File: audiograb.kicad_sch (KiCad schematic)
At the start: 6 parts, among them J1 USB_C_Receptacle_USB2.0_16P, U12 IP4220CZ6F

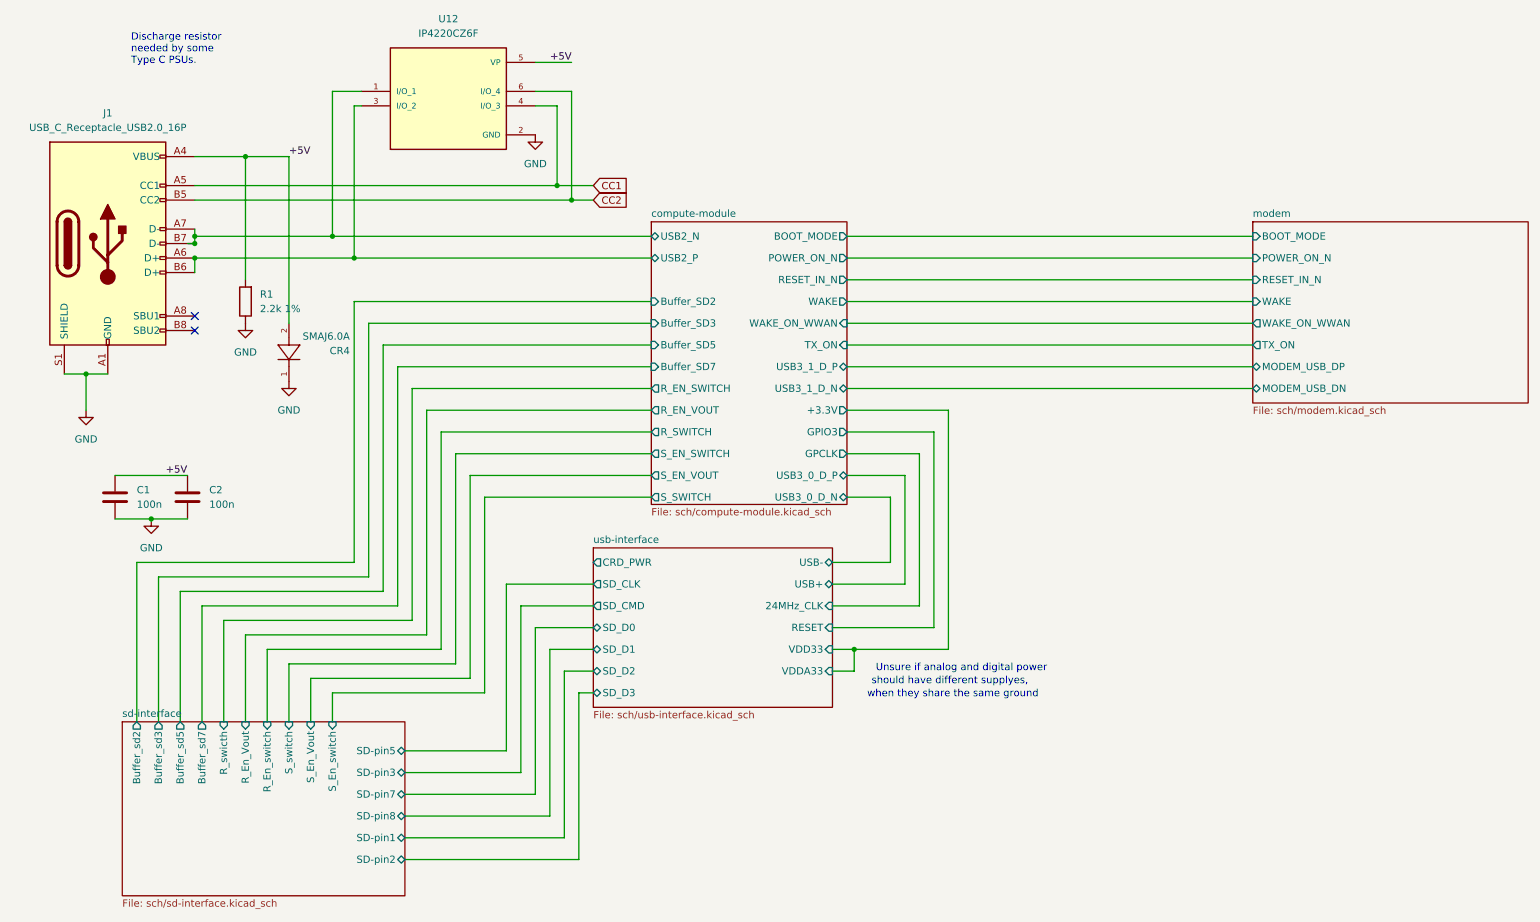
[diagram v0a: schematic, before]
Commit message: added ports to powersupply
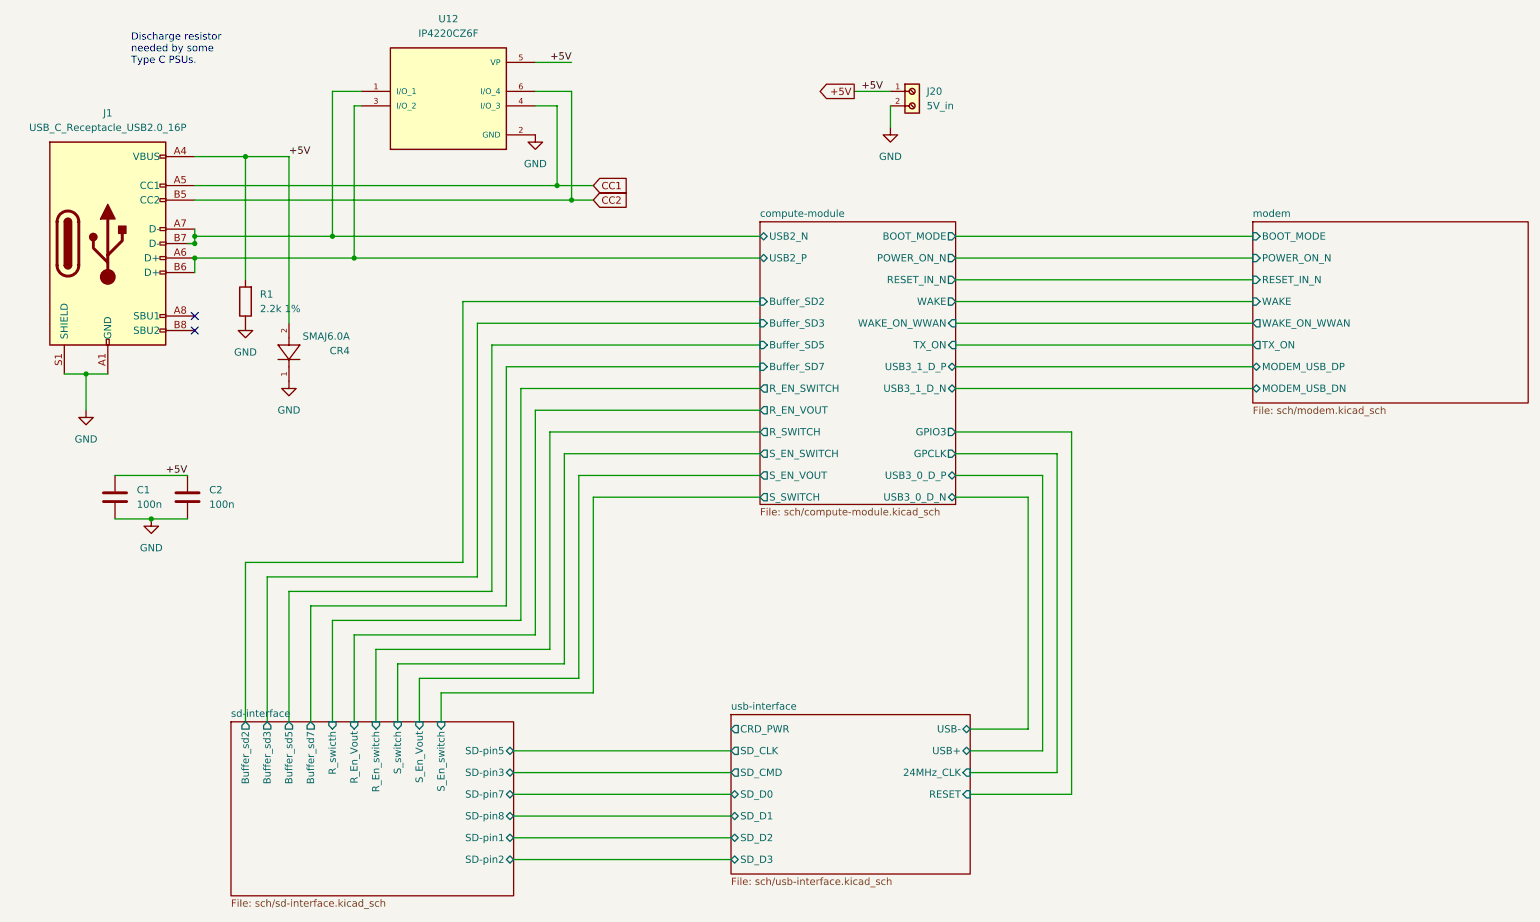
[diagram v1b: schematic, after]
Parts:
- added J20: 5V_in, 691137710002:691137710002, symbol 691137710002:691137710002
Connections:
- net +5V: now also J20.1
- net GND: now also J20.2
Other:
- sheet compute-module ports: added none; removed +3.3V
- sheet usb-interface ports: added none; removed VDD33, VDDA33
- note removed: "Unsure if analog and digital power"
- note removed: "should have different supplyes,"
- note removed: "when they share the same ground"

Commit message: fix annotation and clean up schematics
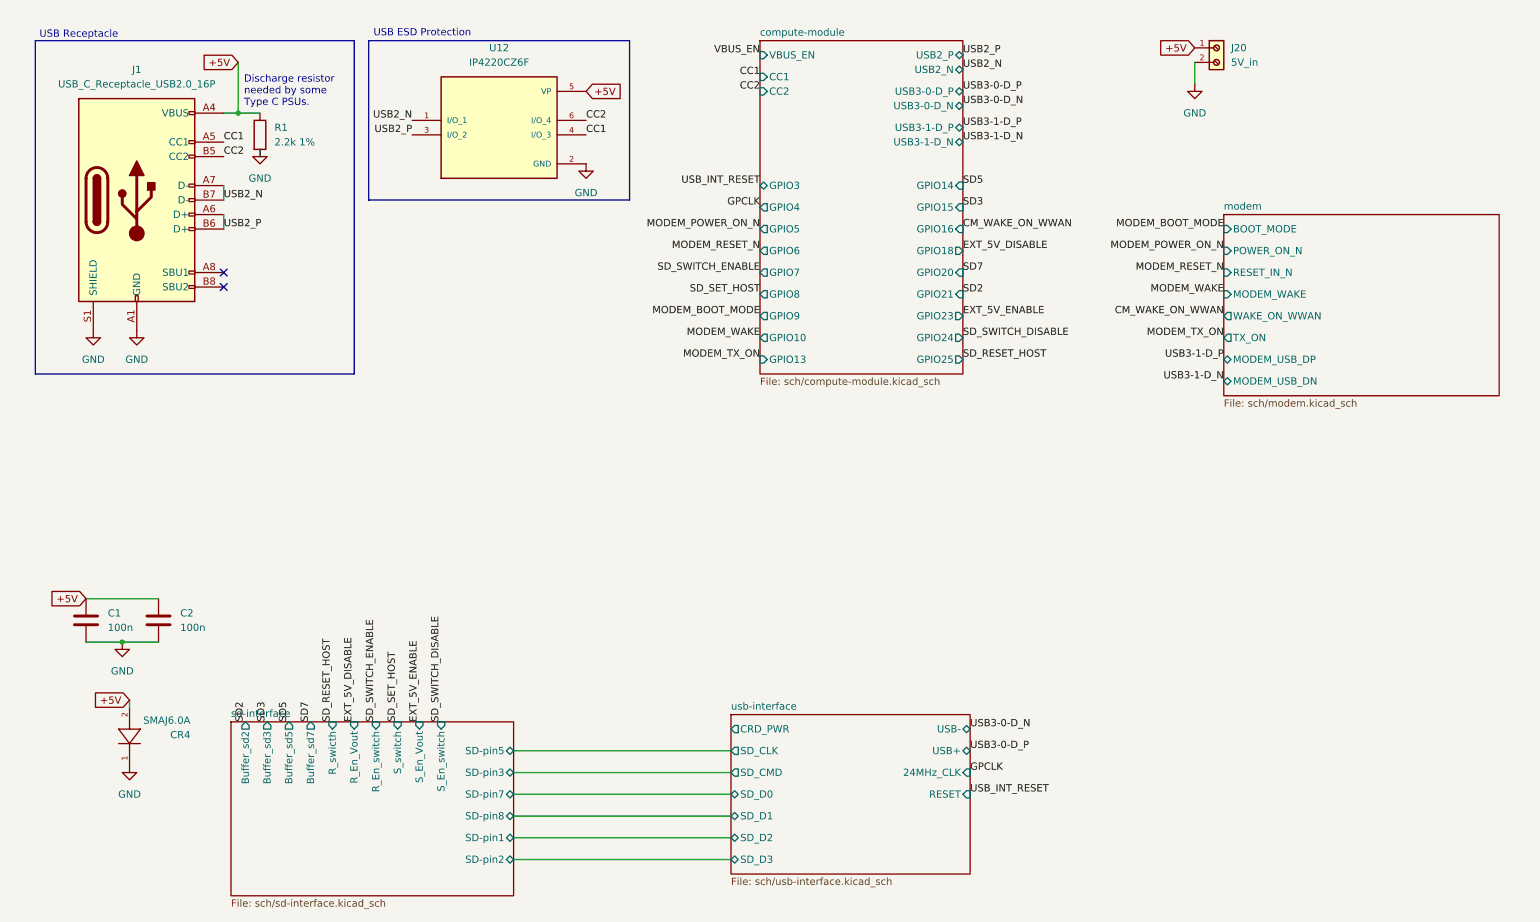
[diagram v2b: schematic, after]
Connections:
- net +5V: now also R1.1; no longer R1.2
- net GND: now also R1.2; no longer R1.1
- net compute-module/USB2_N renamed USB2_N
- net compute-module/USB2_P renamed USB2_P
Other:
- sheet compute-module ports: added CC1, CC2, GPIO10, GPIO13, GPIO14, GPIO15, GPIO16, GPIO18, GPIO20, GPIO21, GPIO23, GPIO24, GPIO25, GPIO4, GPIO5, GPIO6, GPIO7, GPIO8, GPIO9, USB3-0-D_N, USB3-0-D_P, USB3-1-D_N, USB3-1-D_P, VBUS_EN; removed BOOT_MODE, Buffer_SD2, Buffer_SD3, Buffer_SD5, Buffer_SD7, GPCLK, POWER_ON_N, RESET_IN_N, R_EN_SWITCH, R_EN_VOUT, R_SWITCH, S_EN_SWITCH, S_EN_VOUT, S_SWITCH, TX_ON, USB3_0_D_N, USB3_0_D_P, USB3_1_D_N, USB3_1_D_P, WAKE, WAKE_ON_WWAN
- sheet modem ports: added MODEM_WAKE; removed WAKE
- note added: "USB ESD Protection"
- note added: "USB Receptacle"
- moved on the sheet: C1, C2, CR4, J1, J20, R1, U12

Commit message: started pcb design
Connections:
- net CC2: now also U12.3 (I/O_2); no longer U12.6 (I/O_4)
- net USB2_N: now also U12.6 (I/O_4); no longer U12.1 (I/O_1)
- net USB2_P: now also U12.1 (I/O_1); no longer U12.3 (I/O_2)
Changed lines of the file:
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@@
 	)
 	(label "USB2_P"
-		(at 81.28 34.29 180)
+		(at 81.28 31.75 180)
 		(effects
 			(font
@@
 	)
 	(label "CC2"
-		(at 111.76 31.75 0)
-		(effects
-			(font
-				(size 1.27 1.27)
-			)
-			(justify left bottom)
+		(at 81.28 34.29 180)
+		(effects
+			(font
+				(size 1.27 1.27)
+			)
+			(justify right bottom)
 		)
 	)
@@
 	)
 	(label "USB2_N"
-		(at 81.28 31.75 180)
-		(effects
-			(font
-				(size 1.27 1.27)
-			)
-			(justify right bottom)
-		)
-	)
+		(at 111.76 31.75 0)
+		(effects
+			(font
+				(size 1.27 1.27)
+			)
+			(justify left bottom)
+		)
+	)

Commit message: work pcb about 70 percent
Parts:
- removed J20: 5V_in, 691137710002:691137710002, symbol 691137710002:691137710002
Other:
- sheet modem ports: added WAKE_ON_WWAN_port; removed WAKE_ON_WWAN
- note added: "bytta navn for å unngaa label konflikt"

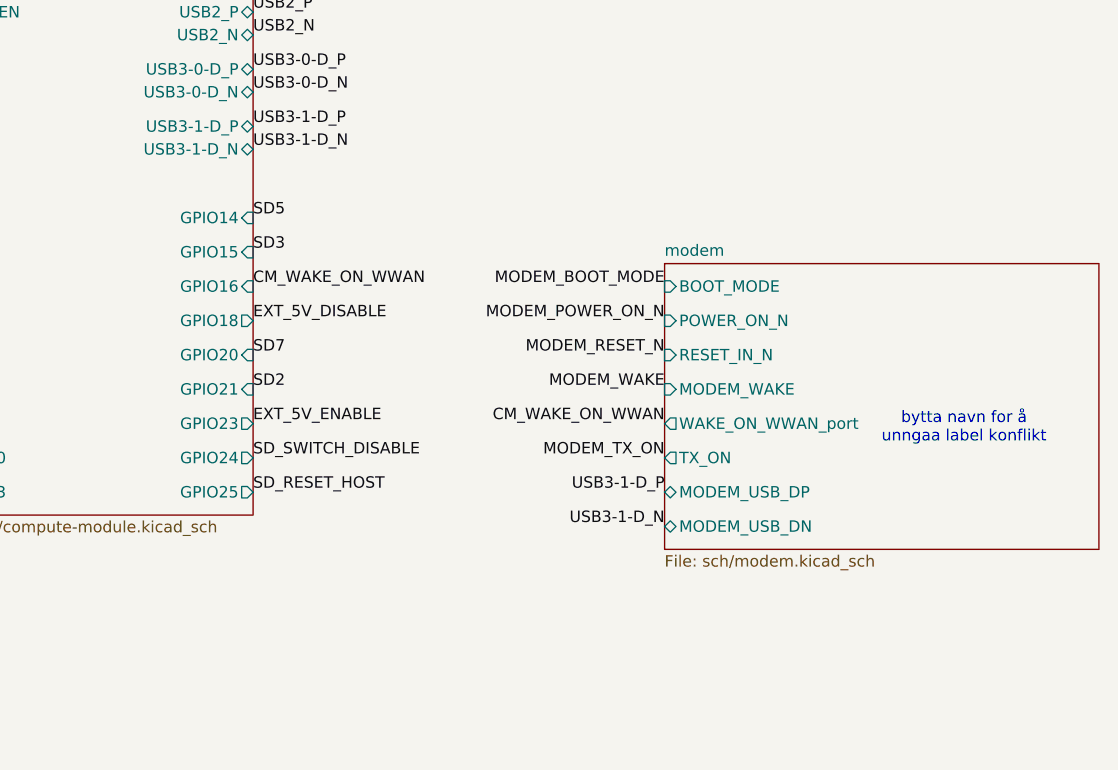
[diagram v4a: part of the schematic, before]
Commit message: partially route the powerlines
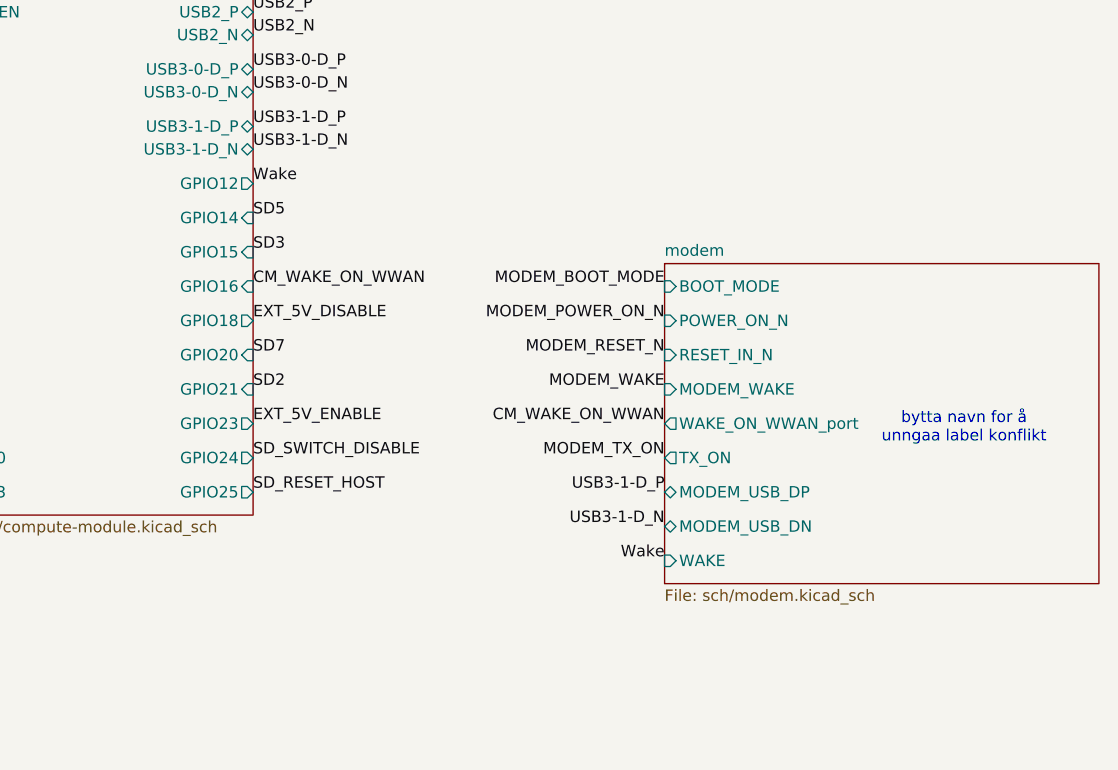
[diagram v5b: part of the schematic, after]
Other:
- sheet compute-module ports: added GPIO12; removed none
- sheet modem ports: added WAKE; removed none
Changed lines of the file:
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@@
+		)
+	)
+	(label "Wake"
+		(at 223.52 81.28 180)
+		(effects
+			(font
+				(size 1.27 1.27)
+			)
+			(justify right bottom)
 		)
 	)
 	(label "SD_RESET_HOST"
 		(at 67.31 137.16 90)
+		(effects
+			(font
+				(size 1.27 1.27)
+			)
+			(justify left bottom)
+		)
+	)
+	(label "Wake"
+		(at 177.8 39.37 0)
 		(effects
 			(font
@@
 	(sheet
 		(at 223.52 48.26)
-		(size 48.26 31.75)
+		(size 48.26 35.56)
 		(exclude_from_sim no)
 		(in_bom yes)
@@
 		)
 		(property "Sheetfile" "sch/modem.kicad_sch"
-			(at 223.52 80.5946 0)
+			(at 223.52 84.4046 0)
 			(effects
 				(font
@@
 		(pin "WAKE_ON_WWAN_port" output
 			(at 223.52 66.04 180)
+			(effects
+				(font
+					(size 1.27 1.27)
+				)
+				(justify left)
+			)
+		)
+		(pin "WAKE" input
+			(at 223.52 81.28 180)
 			(effects
 				(font
@@
 			)
 		)
+		(pin "GPIO12" output
+			(at 177.8 39.37 0)
+			(effects
+				(font
+					(size 1.27 1.27)
+				)
+				(justify right)
+			)
+		)

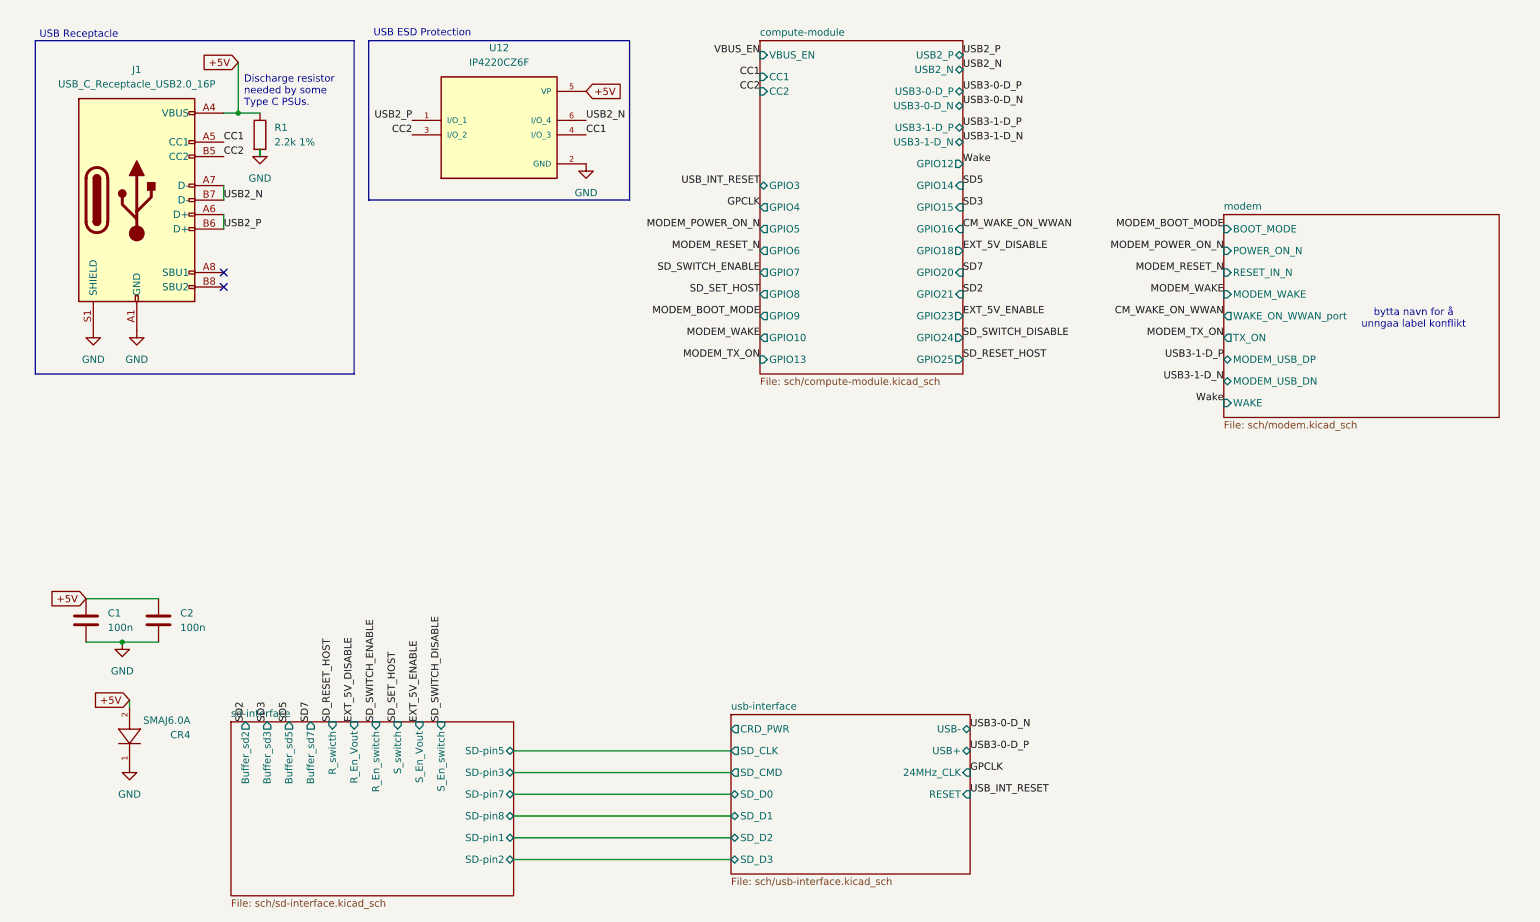
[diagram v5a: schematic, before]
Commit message: powergrid complete, still missing antennas
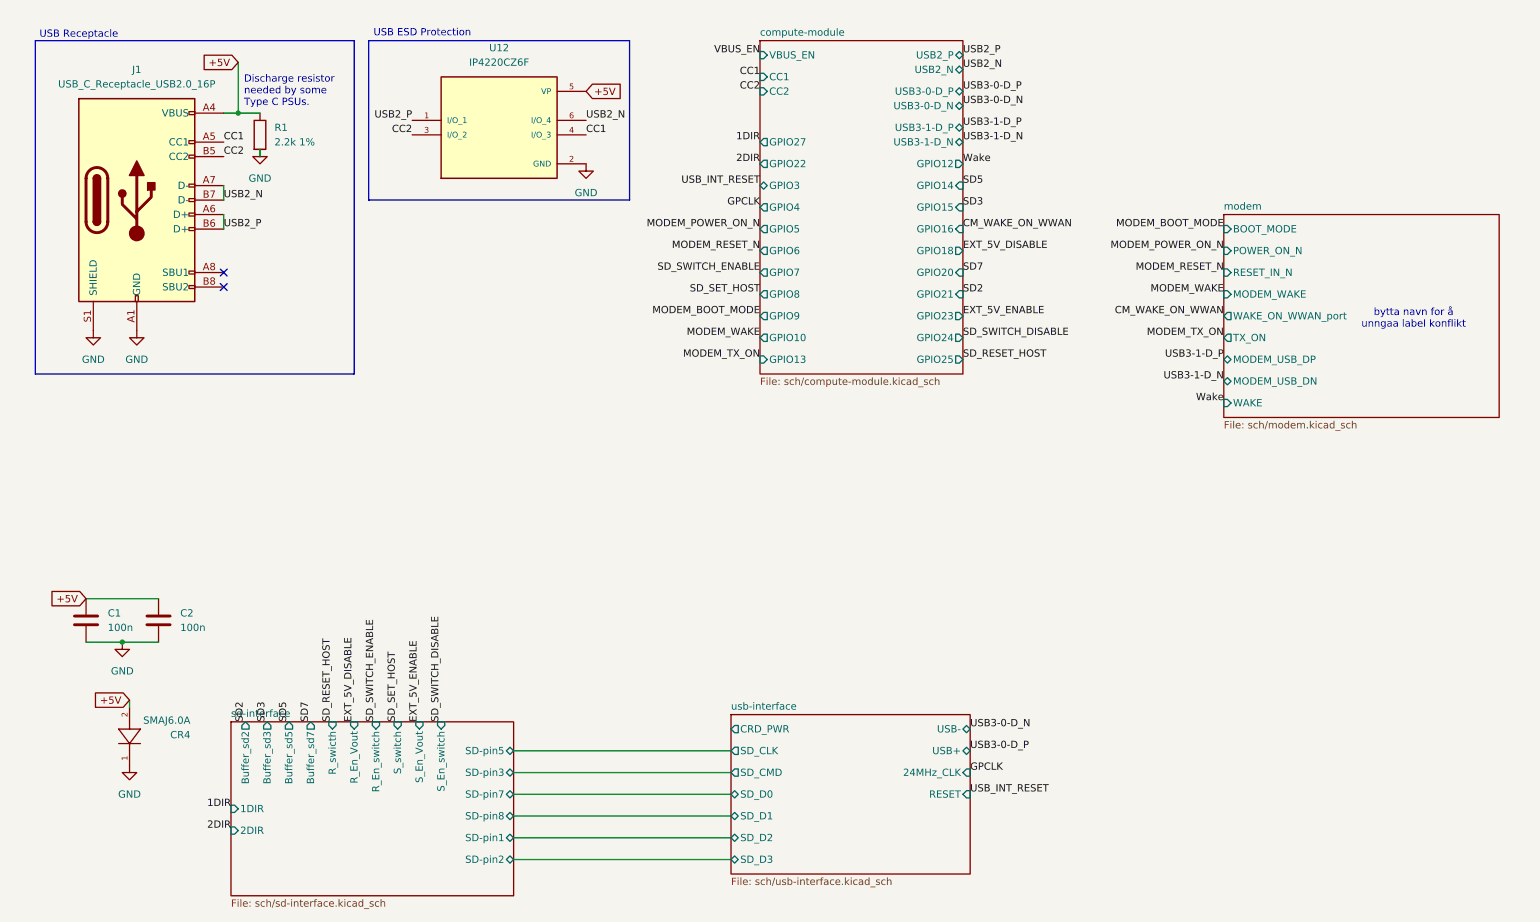
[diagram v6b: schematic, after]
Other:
- sheet compute-module ports: added GPIO22, GPIO27; removed none
- sheet sd-interface ports: added 1DIR, 2DIR; removed none
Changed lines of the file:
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@@
+		)
+	)
+	(label "2DIR"
+		(at 142.24 39.37 180)
+		(effects
+			(font
+				(size 1.27 1.27)
+			)
+			(justify right bottom)
 		)
 	)
@@
 		)
 	)
+	(label "1DIR"
+		(at 142.24 35.56 180)
+		(effects
+			(font
+				(size 1.27 1.27)
+			)
+			(justify right bottom)
+		)
+	)
 	(label "SD_RESET_HOST"
 		(at 177.8 73.66 0)
@@
 		)
 	)
+	(label "2DIR"
+		(at 49.53 156.21 180)
+		(effects
+			(font
+				(size 1.27 1.27)
+			)
+			(justify right bottom)
+		)
+	)
 	(label "MODEM_WAKE"
 		(at 142.24 69.85 180)
@@
 	(label "MODEM_RESET_N"
 		(at 223.52 58.42 180)
+		(effects
+			(font
+				(size 1.27 1.27)
+			)
+			(justify right bottom)
+		)
+	)
+	(label "1DIR"
+		(at 49.53 152.4 180)
 		(effects
 			(font
@@
 			)
 		)
+		(pin "1DIR" input
+			(at 49.53 152.4 180)
+			(effects
+				(font
+					(size 1.27 1.27)
+				)
+				(justify left)
+			)
+		)
+		(pin "2DIR" input
+			(at 49.53 156.21 180)
+			(effects
+				(font
+					(size 1.27 1.27)
+				)
+				(justify left)
+			)
+		)
 		(instances
 			(project "audiograb"
@@
 			)
 		)
+		(pin "GPIO22" output
+			(at 142.24 39.37 180)
+			(effects
+				(font
+					(size 1.27 1.27)
+				)
+				(justify left)
+			)
+		)
+		(pin "GPIO27" output
+			(at 142.24 35.56 180)
+			(effects
+				(font
+					(size 1.27 1.27)
+				)
+				(justify left)
+			)
+		)
